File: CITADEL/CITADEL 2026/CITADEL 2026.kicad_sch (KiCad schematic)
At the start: 43 parts, among them J1 Vibration Motor, J18 CAN BUS, J19 Battery Connections, J2 Stepper 1, J3 LED Strip, J4 Spark Max PWM, J5 Spark Max PWR, J6 Faerie, J7 Stepper 2, P1 PS1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

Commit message: Started PCB V1
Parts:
- removed J3: LED Strip, Connector_JST:JST_EH_B3B-EH-A_1x03_P2.50mm_Vertical, symbol Connector:Conn_01x03_Pin
- added J3: LED Strip, Connector_PinHeader_2.54mm:PinHeader_1x02_P2.54mm_Vertical, symbol Connector:Conn_01x02_Pin
- added R12: 10 kΩ, Resistor_SMD:R_0603_1608Metric_Pad0.98x0.95mm_HandSolder, symbol Device:R
- added S1: Push Button, Jayse_Footprints:SW_TS02-66-60-BK-100-SCR-D, symbol TS02-66-60-BK-100-SCR-D:TS02-66-60-BK-100-SCR-D
- J18, J6: footprint Connector_AMASS:AMASS_XT30U-F_1x02_P5.0mm_Vertical -> Connector_AMASS:AMASS_XT30U-M_1x02_P5.0mm_Vertical
- J4: footprint Connector_JST:JST_EH_B2B-EH-A_1x02_P2.50mm_Vertical -> Connector_PinHeader_2.54mm:PinHeader_1x02_P2.54mm_Vertical
- J5: footprint Connector_AMASS:AMASS_XT30U-F_1x02_P5.0mm_Vertical -> Connector_AMASS:AMASS_XT60-M_1x02_P7.20mm_Vertical
- MG90S3: value MG90S 4 -> MG90S 3
- MG90S4: value MG90S 5 -> MG90S 4
- MG90S5: value MG90S 6 -> MG90S 5
- MG90S6: value MG90S 3 -> MG90S 6
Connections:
- net LED_Strip is gone; now on net Stepper2_STEP: U4.J1_8 (GPIO15)
- net +3.3V: now also R12.1
- net +5V: now also J3.2 (Pin_2)
- net 5V_ADC: now also U4.J1_4 (GPIO4); no longer U4.J1_6 (GPIO6)
- net BATT_ADC: now also U4.J1_6 (GPIO6); no longer U4.J1_4 (GPIO4)
- net CRX_ESP: now also U4.J1_17 (GPIO11); no longer U4.J1_10 (GPIO17)
- net CTX_ESP: now also U4.J1_18 (GPIO12); no longer U4.J1_11 (GPIO18)
- net GND: now also J3.1 (Pin_1), S1.2, S1.4
- net MG90S1: now also U4.J3_10 (GPIO38); no longer U4.J3_4 (GPIO1)
- net MG90S2: now also U4.J3_11 (GPIO37); no longer U4.J3_5 (GPIO2)
- net MG90S3: now also MG90S3.1 (PWM), U4.J3_12 (GPIO36); no longer MG90S6.1 (PWM), U4.J3_6 (MTMS/GPIO42)
- net MG90S4: now also MG90S4.1 (PWM); no longer MG90S3.1 (PWM)
- net MG90S5: now also MG90S5.1 (PWM); no longer MG90S4.1 (PWM)
- net MG90S6: now also MG90S6.1 (PWM); no longer MG90S5.1 (PWM)
- net MG90S7: now also U4.J3_4 (GPIO1); no longer U4.J3_10 (GPIO38)
- net MG90S8: now also U4.J3_5 (GPIO2); no longer U4.J3_11 (GPIO37)
- net MG90S9: now also U4.J3_6 (MTMS/GPIO42); no longer U4.J3_12 (GPIO36)
- net Motor1_2: now also J2.3 (Pin_3); no longer J2.2 (Pin_2)
- net Motor1_3: now also J2.2 (Pin_2); no longer J2.3 (Pin_3)
- net Motor2_2: now also J7.3 (Pin_3); no longer J7.2 (Pin_2)
- net Motor2_3: now also J7.2 (Pin_2); no longer J7.3 (Pin_3)
- net Spark_Max_PWM: now also U4.J1_16 (GPIO10); no longer U4.J1_9 (GPIO16)
- net Stepper1_STEP: now also U4.J1_10 (GPIO17); no longer U4.J1_14 (GPIO46)
- net Stepper2_STEP: no longer U4.J1_15 (GPIO9)
- net Stepper_DIR: now also U4.J1_9 (GPIO16); no longer U4.J1_13 (GPIO3)
- net Stepper_EN: now also U4.J1_14 (GPIO46); no longer U4.J1_12 (GPIO8)
- net Stepper_M0: now also U4.J1_13 (GPIO3); no longer U4.J1_16 (GPIO10)
- net Stepper_M1: now also U4.J1_12 (GPIO8); no longer U4.J1_17 (GPIO11)
- net Stepper_M2: now also U4.J1_11 (GPIO18); no longer U4.J1_18 (GPIO12)
- new net Button: R12.2, S1.1, S1.3, U4.J1_15 (GPIO9)
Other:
- note added: "Push Button"

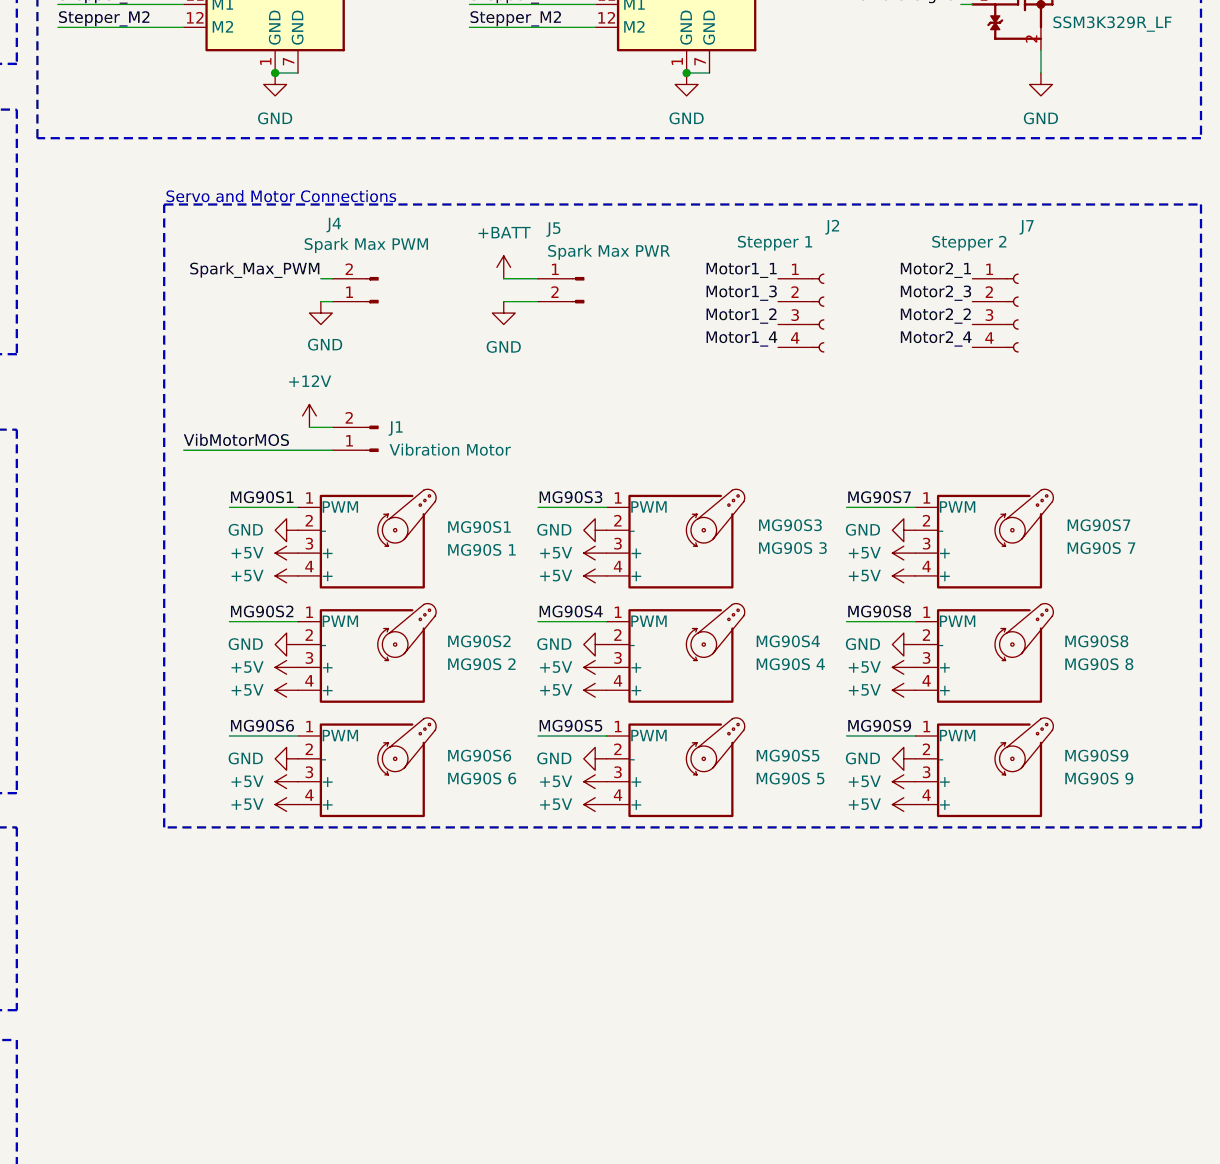
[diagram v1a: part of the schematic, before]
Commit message: Added camera connectors
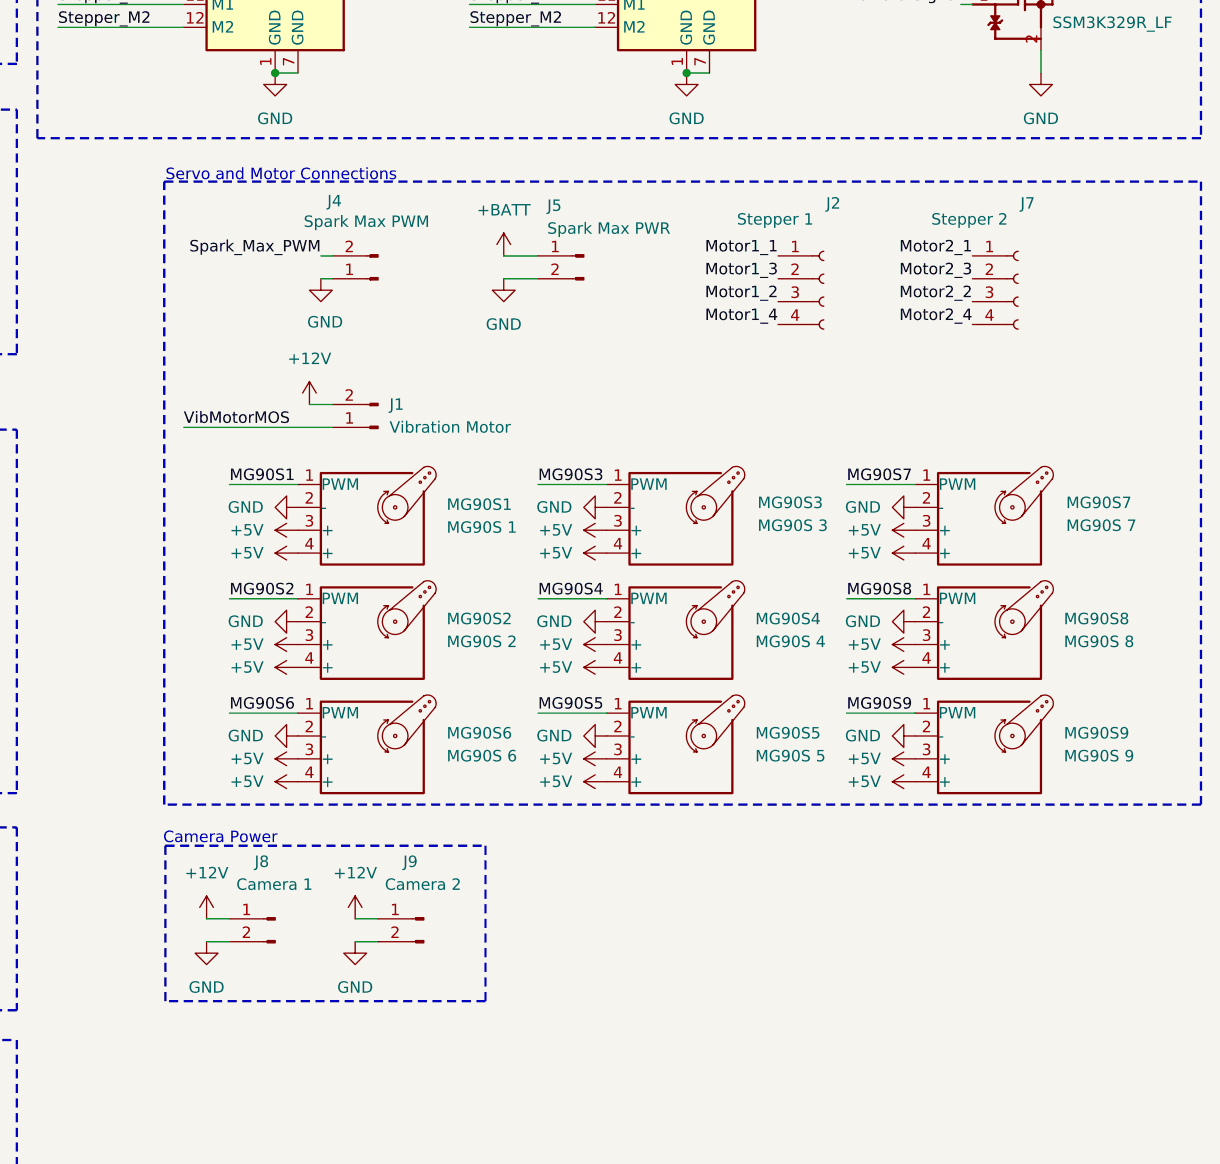
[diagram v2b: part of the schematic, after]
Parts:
- added J8: Camera 1, Connector_AMASS:AMASS_XT30U-M_1x02_P5.0mm_Vertical, symbol Connector:Conn_01x02_Pin
- added J9: Camera 2, Connector_AMASS:AMASS_XT30U-M_1x02_P5.0mm_Vertical, symbol Connector:Conn_01x02_Pin
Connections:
- net +12V: now also J8.1 (Pin_1), J9.1 (Pin_1)
- net GND: now also J8.2 (Pin_2), J9.2 (Pin_2)
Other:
- note added: "Camera Power"
- moved on the sheet: J1, J2, J4, J5, J7, MG90S1, MG90S2, MG90S3, MG90S4, MG90S5, MG90S6, MG90S7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

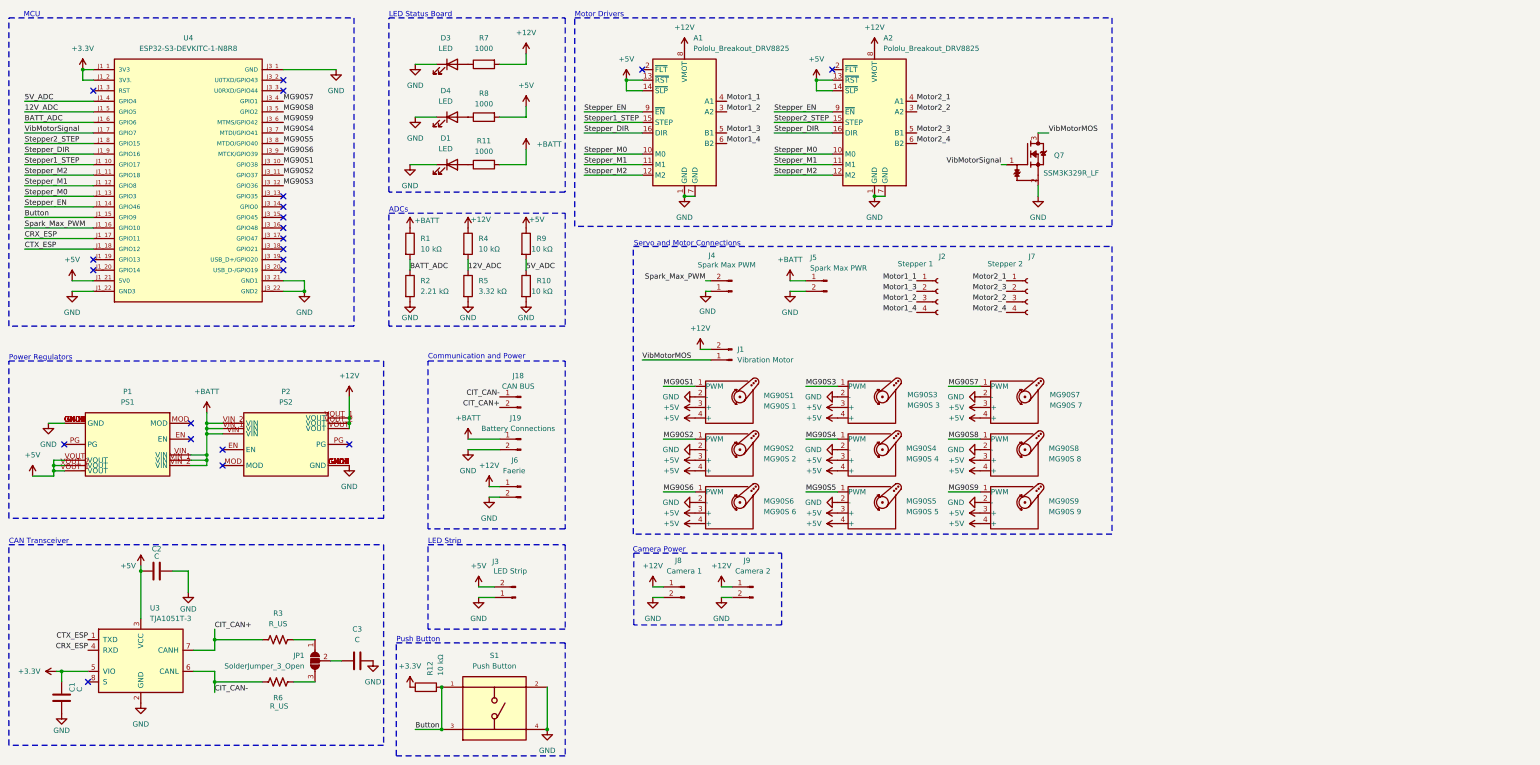
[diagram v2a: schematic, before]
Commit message: Changed servo connectors, added connector for servo daughter board
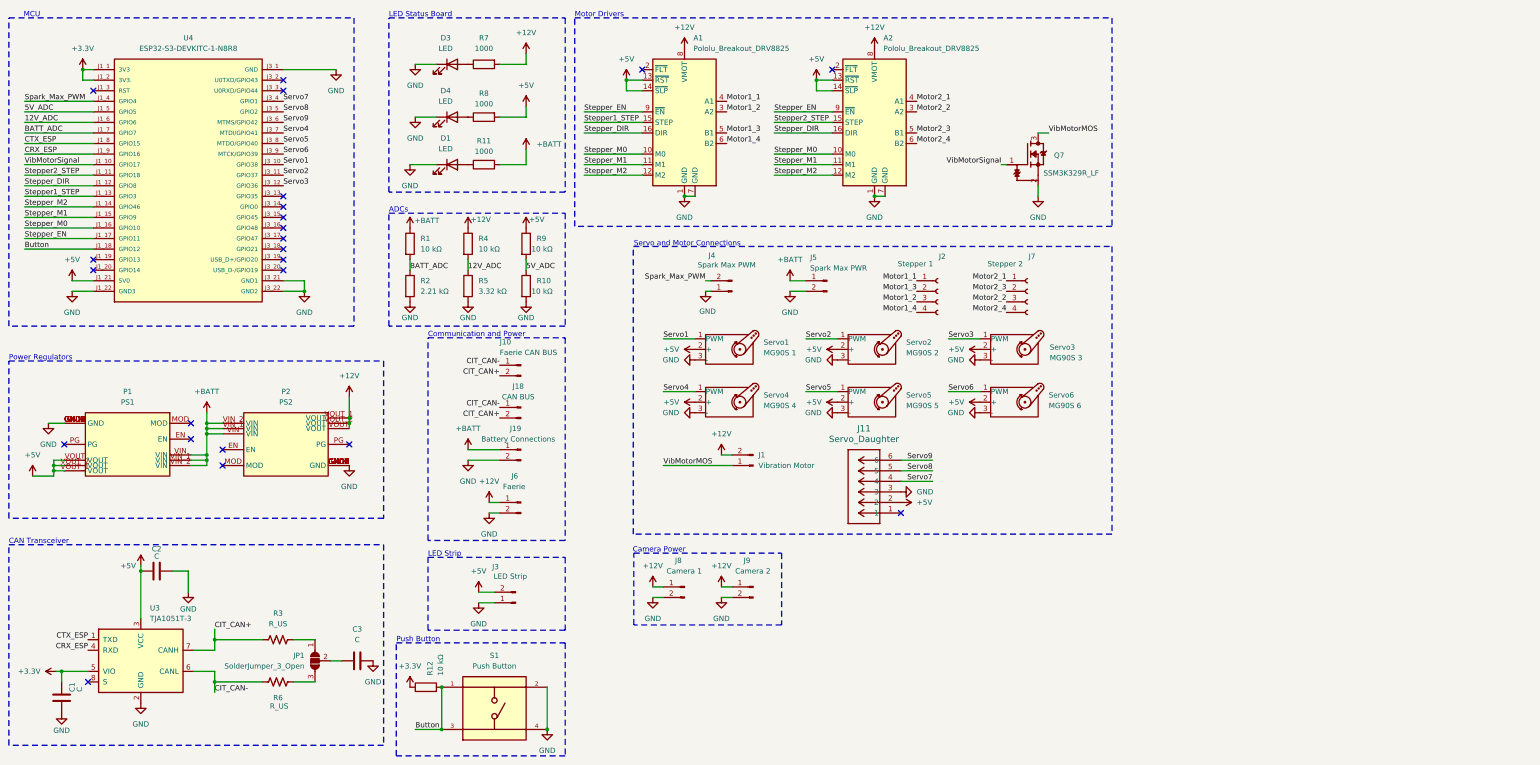
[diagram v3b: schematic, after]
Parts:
- removed MG90S7: MG90S 7, Connector_Molex:Molex_Mini-Fit_Jr_5566-04A_2x02_P4.20mm_Vertical, symbol Motor:Motor_Servo
- removed MG90S8: MG90S 8, Connector_Molex:Molex_Mini-Fit_Jr_5566-04A_2x02_P4.20mm_Vertical, symbol Motor:Motor_Servo
- removed MG90S9: MG90S 9, Connector_Molex:Molex_Mini-Fit_Jr_5566-04A_2x02_P4.20mm_Vertical, symbol Motor:Motor_Servo
- added J10: Faerie CAN BUS, Connector_AMASS:AMASS_XT30U-M_1x02_P5.0mm_Vertical, symbol Connector:Conn_01x02_Pin
- added J11: Servo_Daughter, Jayse_Footprints:CONN_SD-5566-002_06_MOL, symbol 2026-01-24_03-47-07:39281063
- Servo1: renamed from MG90S1; footprint Connector_Molex:Molex_Mini-Fit_Jr_5566-04A_2x02_P4.20mm_Vertical -> Connector_PinHeader_2.54mm:PinHeader_1x03_P2.54mm_Vertical
- Servo2: renamed from MG90S2; footprint Connector_Molex:Molex_Mini-Fit_Jr_5566-04A_2x02_P4.20mm_Vertical -> Connector_PinHeader_2.54mm:PinHeader_1x03_P2.54mm_Vertical
- Servo3: renamed from MG90S3; footprint Connector_Molex:Molex_Mini-Fit_Jr_5566-04A_2x02_P4.20mm_Vertical -> Connector_PinHeader_2.54mm:PinHeader_1x03_P2.54mm_Vertical
- Servo4: renamed from MG90S4; footprint Connector_Molex:Molex_Mini-Fit_Jr_5566-04A_2x02_P4.20mm_Vertical -> Connector_PinHeader_2.54mm:PinHeader_1x03_P2.54mm_Vertical
- Servo5: renamed from MG90S5; footprint Connector_Molex:Molex_Mini-Fit_Jr_5566-04A_2x02_P4.20mm_Vertical -> Connector_PinHeader_2.54mm:PinHeader_1x03_P2.54mm_Vertical
- Servo6: renamed from MG90S6; footprint Connector_Molex:Molex_Mini-Fit_Jr_5566-04A_2x02_P4.20mm_Vertical -> Connector_PinHeader_2.54mm:PinHeader_1x03_P2.54mm_Vertical
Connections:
- net +5V: now also Servo1.2 (+), Servo2.2 (+), Servo3.2 (+), Servo4.2 (+), Servo5.2 (+), Servo6.2 (+), J11.2; no longer Servo1.3 (+), Servo1.4 (+), Servo2.3 (+), Servo2.4 (+), Servo3.3 (+), Servo3.4 (+), Servo4.3 (+), Servo4.4 (+), Servo5.3 (+), Servo5.4 (+), Servo6.3 (+), Servo6.4 (+)
- net 12V_ADC: now also U4.J1_6 (GPIO6); no longer U4.J1_5 (GPIO5)
- net 5V_ADC: now also U4.J1_5 (GPIO5); no longer U4.J1_4 (GPIO4)
- net BATT_ADC: now also U4.J1_7 (GPIO7); no longer U4.J1_6 (GPIO6)
- net Button: now also U4.J1_18 (GPIO12); no longer U4.J1_15 (GPIO9)
- net CIT_CAN+: now also J10.2 (Pin_2)
- net CIT_CAN-: now also J10.1 (Pin_1)
- net CRX_ESP: now also U4.J1_9 (GPIO16); no longer U4.J1_17 (GPIO11)
- net CTX_ESP: now also U4.J1_8 (GPIO15); no longer U4.J1_18 (GPIO12)
- net GND: now also Servo1.3 (-), Servo2.3 (-), Servo3.3 (-), Servo4.3 (-), Servo5.3 (-), Servo6.3 (-), J11.3; no longer Servo1.2 (-), Servo2.2 (-), Servo3.2 (-), Servo4.2 (-), Servo5.2 (-), Servo6.2 (-)
- net Spark_Max_PWM: now also U4.J1_4 (GPIO4); no longer U4.J1_16 (GPIO10)
- net Stepper1_STEP: now also U4.J1_13 (GPIO3); no longer U4.J1_10 (GPIO17)
- net Stepper2_STEP: now also U4.J1_11 (GPIO18); no longer U4.J1_8 (GPIO15)
- net Stepper_DIR: now also U4.J1_12 (GPIO8); no longer U4.J1_9 (GPIO16)
- net Stepper_EN: now also U4.J1_17 (GPIO11); no longer U4.J1_14 (GPIO46)
- net Stepper_M0: now also U4.J1_16 (GPIO10); no longer U4.J1_13 (GPIO3)
- net Stepper_M1: now also U4.J1_15 (GPIO9); no longer U4.J1_12 (GPIO8)
- net Stepper_M2: now also U4.J1_14 (GPIO46); no longer U4.J1_11 (GPIO18)
- net VibMotorSignal: now also U4.J1_10 (GPIO17); no longer U4.J1_7 (GPIO7)
- net MG90S1 renamed Servo1
- net MG90S2 renamed Servo2
- net MG90S3 renamed Servo3
- net MG90S4 renamed Servo4
- net MG90S5 renamed Servo5
- net MG90S6 renamed Servo6
- net MG90S7 renamed Servo7
- net Servo7: now also J11.4
- net MG90S8 renamed Servo8
- net Servo8: now also J11.5
- net MG90S9 renamed Servo9
- net Servo9: now also J11.6
- no-connect marks 22 -> 23
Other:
- moved on the sheet: J1, J18, J19, J3, J6

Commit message: Added PCA9685 servo controller
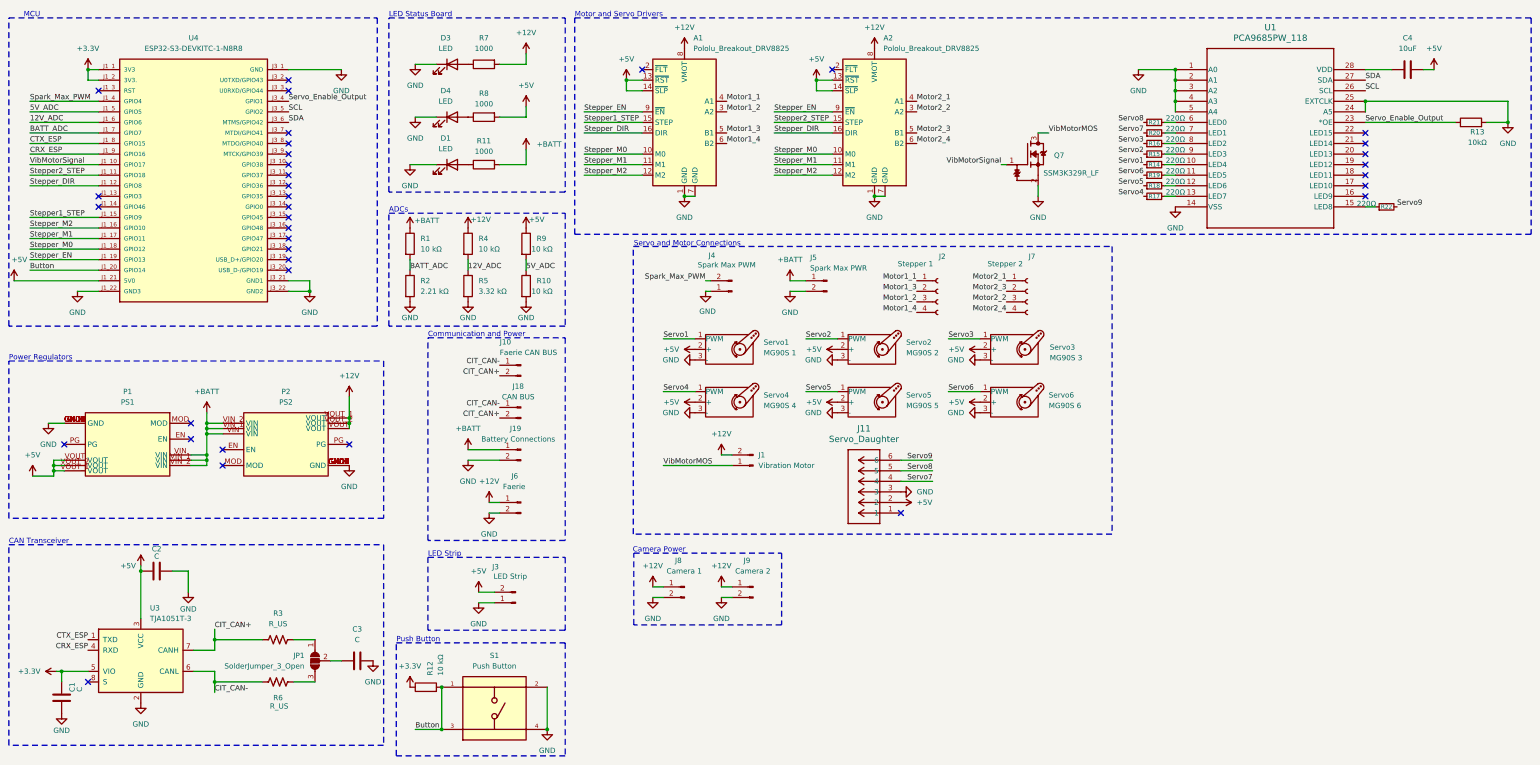
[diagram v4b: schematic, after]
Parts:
- added C4: 10uF, Capacitor_SMD:C_0603_1608Metric_Pad1.08x0.95mm_HandSolder, symbol Device:C
- added R13: 10kΩ, Resistor_SMD:R_0603_1608Metric_Pad0.98x0.95mm_HandSolder, symbol Device:R
- added R14, R15, R16, R17, R18, R19, R20, R21, R22: 220Ω, Resistor_SMD:R_0603_1608Metric_Pad0.98x0.95mm_HandSolder, symbol Device:R_Small
- added U1: PCA9685PW_118, Jayse_Footprints:TSSOP28_SOT361-1_NXP, symbol 2026-01-29_22-26-42:PCA9685PW_118
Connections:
- net +5V: now also C4.2
- net Button: now also U4.J1_20 (GPIO14); no longer U4.J1_18 (GPIO12)
- net GND: now also R13.2, U1.1 (A0), U1.14 (VSS), U1.2 (A1), U1.24 (A5), U1.25 (EXTCLK), U1.3 (A2), U1.4 (A3), U1.5 (A4)
- net Servo1: now also R14.1; no longer U4.J3_10 (GPIO38)
- net Servo2: now also R15.1; no longer U4.J3_11 (GPIO37)
- net Servo3: now also R16.1; no longer U4.J3_12 (GPIO36)
- net Servo4: now also R17.1; no longer U4.J3_7 (MTDI/GPIO41)
- net Servo5: now also R18.1; no longer U4.J3_8 (MTDO/GPIO40)
- net Servo6: now also R19.1; no longer U4.J3_9 (MTCK/GPIO39)
- net Servo7: now also R20.1; no longer U4.J3_4 (GPIO1)
- net Servo8: now also R21.1; no longer U4.J3_5 (GPIO2)
- net Servo9: now also R22.2; no longer U4.J3_6 (MTMS/GPIO42)
- net Stepper1_STEP: now also U4.J1_15 (GPIO9); no longer U4.J1_13 (GPIO3)
- net Stepper_EN: now also U4.J1_19 (GPIO13); no longer U4.J1_17 (GPIO11)
- net Stepper_M0: now also U4.J1_18 (GPIO12); no longer U4.J1_16 (GPIO10)
- net Stepper_M1: now also U4.J1_17 (GPIO11); no longer U4.J1_15 (GPIO9)
- net Stepper_M2: now also U4.J1_16 (GPIO10); no longer U4.J1_14 (GPIO46)
- new net: R14.2, U1.10 (LED4)
- new net: R21.2, U1.6 (LED0)
- new net: R19.2, U1.11 (LED5)
- new net: R20.2, U1.7 (LED1)
- new net: R16.2, U1.8 (LED2)
- new net: R18.2, U1.12 (LED6)
- new net: C4.1, U1.28 (VDD)
- new net: R15.2, U1.9 (LED3)
- new net: R17.2, U1.13 (LED7)
- new net: R22.1, U1.15 (LED8)
- new net SCL: U1.26 (SCL), U4.J3_5 (GPIO2)
- new net SDA: U1.27 (SDA), U4.J3_6 (MTMS/GPIO42)
- new net Servo_Enable_Output: R13.1, U1.23 (*OE), U4.J3_4 (GPIO1)
- no-connect marks 23 -> 36
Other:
- note added: "Motor and Servo Drivers"
- note removed: "Motor Drivers"
- moved on the sheet: U4
